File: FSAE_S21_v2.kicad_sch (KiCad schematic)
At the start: 75 parts

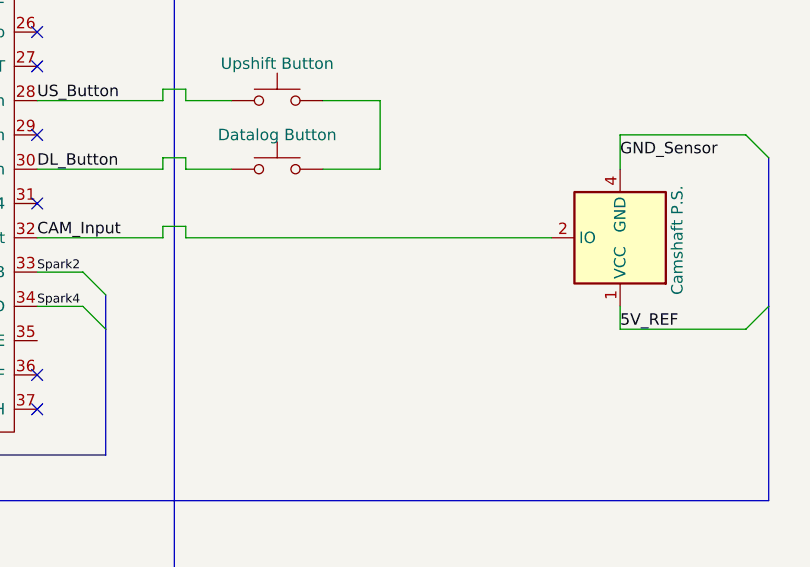
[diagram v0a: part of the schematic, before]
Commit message: added pullup resistor to cam
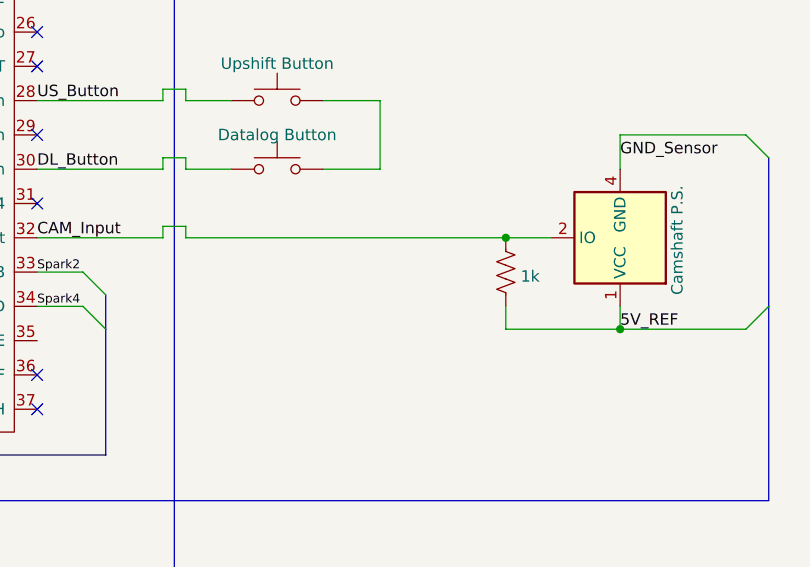
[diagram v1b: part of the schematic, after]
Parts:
- added R?: 1k, symbol Device:R_US
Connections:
- net 5V_REF: now also R?.1
- net CAM_Input: now also R?.2
- new net: F?.1, U?.~ (VCC), U?.~ (VCC), U?.~ (VCC), U?.~ (VCC)
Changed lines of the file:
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@@
   (junction (at 104.14 93.98) (diameter 0) (color 0 0 0 0)
   )
+  (junction (at 468.63 83.82) (diameter 0) (color 0 0 0 0)
+  )
   (junction (at 363.22 97.79) (diameter 0) (color 0 0 0 0)
   )
@@
   (junction (at 445.77 248.92) (diameter 0) (color 0 0 0 0)
   )
+  (junction (at 455.93 73.66) (diameter 0) (color 0 0 0 0)
+  )
   (junction (at 91.44 104.14) (diameter 0) (color 0 0 0 0)
   )
@@
     (stroke (width 0) (type default) (color 0 0 0 0))
   )
-  (wire (pts (xy 420.37 73.66) (xy 461.01 73.66))
-    (stroke (width 0) (type default) (color 0 0 0 0))
-  )
   (bus (pts (xy 345.44 38.1) (xy 345.44 36.83))
     (stroke (width 0) (type default) (color 0 0 0 0))
@@
     (stroke (width 0) (type default) (color 0 0 0 0))
   )
+  (wire (pts (xy 455.93 81.28) (xy 455.93 83.82))
+    (stroke (width 0) (type default) (color 0 0 0 0))
+  )
   (wire (pts (xy 454.66 167.64) (xy 454.66 165.1))
     (stroke (width 0) (type default) (color 0 0 0 0))
@@
     (stroke (width 0) (type default) (color 0 0 0 0))
   )
+  (wire (pts (xy 420.37 73.66) (xy 455.93 73.66))
+    (stroke (width 0) (type default) (color 0 0 0 0))
+  )
   (wire (pts (xy 105.41 160.02) (xy 110.49 160.02))
     (stroke (width 0) (type default) (color 0 0 0 0))
@@
     (stroke (width 0) (type default) (color 0 0 0 0))
   )
+  (wire (pts (xy 455.93 73.66) (xy 461.01 73.66))
+    (stroke (width 0) (type default) (color 0 0 0 0))
+  )
   (bus (pts (xy 347.98 102.87) (xy 485.14 102.87))
     (stroke (width 0) (type default) (color 0 0 0 0))
@@
     (stroke (width 0) (type default) (color 0 0 0 0))
   )
+  (wire (pts (xy 455.93 83.82) (xy 468.63 83.82))
+    (stroke (width 0) (type default) (color 0 0 0 0))
+  )
   (bus (pts (xy 417.83 222.25) (xy 438.15 222.25))
     (stroke (width 0) (type default) (color 0 0 0 0))
@@
     (pin "~")
   )
+  (symbol (lib_id "Device:R_US") (at 455.93 77.47 180) (unit 1)
+    (in_bom yes) (on_board yes) (fields_autoplaced)
+    (property "Reference" "R?" (id 0) (at 451.0745 77.47 90)
+      (effects (font (size 1.27 1.27)) hide)
+    )
+    (property "Value" "1k" (id 1) (at 457.581 77.949 0)
+      (effects (font (size 1.27 1.27)) (justify right))
+    )
+    (property "Footprint" "" (id 2) (at 454.914 77.216 90)
+      (effects (font (size 1.27 1.27)) hide)
+    )
+    (property "Datasheet" "~" (id 3) (at 455.93 77.47 0)
+      (effects (font (size 1.27 1.27)) hide)
+    )
+    (pin "1")
+    (pin "2")
+  )
   (symbol (lib_id "Device:Fuse") (at 114.3 104.14 270) (unit 1)
     (in_bom yes) (on_board yes)
@@
       (reference "M?") (unit 1) (value "Fan") (footprint "")
     )
+    (path "/975284c0-be9d-4c3a-9f49-76e7932b7001"
+      (reference "R?") (unit 1) (value "1k") (footprint "")
+    )
     (path "/e4d4909d-5947-443f-adb6-8e13c916b979"

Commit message: color updates!
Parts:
- F?: value Fuse (5 A?) -> Fuse (3 A)
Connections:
- new net: F?.1, U?.~ (VCC), U?.~ (VCC), U?.~ (VCC), U?.~ (VCC)
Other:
- note added: "Note: Add IMU stuff"
- note added: "Note: Add Telemetry stuff as well"
- note removed: "NOTE: CHECK WITH MASON ABOUT FUSE RATING"
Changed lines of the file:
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@@
   )
   (wire (pts (xy 118.11 104.14) (xy 128.27 104.14))
-    (stroke (width 0) (type default) (color 0 0 0 0))
+    (stroke (width 0) (type default) (color 255 0 0 1))
   )
   (wire (pts (xy 556.26 146.05) (xy 556.26 153.67))
@@
   )
   (wire (pts (xy 118.11 182.88) (xy 128.27 182.88))
-    (stroke (width 0) (type default) (color 0 0 0 0))
+    (stroke (width 0) (type default) (color 255 0 0 1))
   )
   (wire (pts (xy 420.37 118.11) (xy 420.37 119.38))
@@
   )
   (wire (pts (xy 118.11 81.28) (xy 128.27 81.28))
-    (stroke (width 0) (type default) (color 0 0 0 0))
+    (stroke (width 0) (type default) (color 255 0 0 1))
   )
   (bus (pts (xy 121.92 95.25) (xy 121.92 92.71))
@@
   )
   (wire (pts (xy 118.11 134.62) (xy 128.27 134.62))
-    (stroke (width 0) (type default) (color 0 0 0 0))
+    (stroke (width 0) (type default) (color 255 0 0 1))
   )
   (wire (pts (xy 163.83 24.13) (xy 163.83 35.56))
@@
   )
   (wire (pts (xy 118.11 160.02) (xy 128.27 160.02))
-    (stroke (width 0) (type default) (color 0 0 0 0))
+    (stroke (width 0) (type default) (color 255 0 0 1))
   )
   (wire (pts (xy 104.14 71.12) (xy 104.14 76.2))
@@
     )
   )
-  (text "NOTE: CHECK WITH MASON ABOUT FUSE RATING\n\n" (at 99.06 24.13 0)
-    (effects (font (size 1.27 1.27)) (justify left bottom))
-  )
   (text "NOTE: CHECK WITH PI/DISPLAY DATASHEET ABOUT FUSE RATING"
     (at 146.05 191.77 0)
@@
     (effects (font (size 1.27 1.27)) (justify left bottom))
   )
+  (text "Note: Add IMU stuff\n" (at 143.51 214.63 0)
+    (effects (font (size 1.27 1.27)) (justify left bottom))
+  )
   (text "Note: So hopefully the alternator doesn’t put out a lot of \ncurrent that would kill the electronics within the Accessory \nRelay when shut off (i mean it’s fused so should be fine?)\n\nIdea: Rather than putting PKS on the + side of battery, \nput it on negative side so when switch is off then you\nremove the ground?"
     (at 13.97 63.5 0)
@@
     (effects (font (size 1.27 1.27)) (justify left bottom))
   )
+  (text "Note: Add Telemetry stuff as well" (at 147.32 218.44 0)
+    (effects (font (size 1.27 1.27)) (justify left bottom))
+  )
   (text "NOTE: UPDATE PKS WIRING\n" (at 54.61 24.13 0)
     (effects (font (size 1.27 1.27)) (justify left bottom))
@@
     (effects (font (size 1.27 1.27)) (justify right bottom))
   )
-  (label "V_CKS" (at 104.14 172.72 0)
-    (effects (font (size 1.27 1.27)) (justify left bottom))
-  )
   (label "Oil Temp" (at 403.86 35.56 0)
     (effects (font (size 1.27 1.27)) (justify left bottom))
@@
     (effects (font (size 1 1)) (justify left bottom))
   )
+  (label "V_CKS" (at 104.14 177.8 0)
+    (effects (font (size 1.27 1.27)) (justify left bottom))
+  )
   (label "V_PKS" (at 91.44 81.28 0)
     (effects (font (size 1.27 1.27)) (justify left bottom))
@@
       (effects (font (size 1.27 1.27)) hide)
     )
-    (property "Value" "Fuse (5 A?)" (id 1) (at 111.76 24.13 90))
+    (property "Value" "Fuse (3 A)" (id 1) (at 111.76 24.13 90))
     (property "Footprint" "" (id 2) (at 111.76 24.892 90)
       (effects (font (size 1.27 1.27)) hide)
@@
     )
     (path "/37a79518-9db7-49ec-b1d5-f0bef43022e8"
-      (reference "F?") (unit 1) (value "Fuse (5 A?)") (footprint "")
+      (reference "F?") (unit 1) (value "Fuse (3 A)") (footprint "")
     )
     (path "/54a95d73-bd3e-4107-8402-74b486ffb482"

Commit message: remove main relay
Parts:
- removed F?: Fuse (7.5 A), symbol Device:Fuse
- removed K?: Main Relay, Relay_THT:Relay_SPST_StandexMeder_SIL_Form1A, symbol Relay:SILxx-1Axx-71x
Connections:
- net V_PKS: now also F?.2, F?.2
- new net: F?.1, U?.~ (VCC), U?.~ (VCC), U?.~ (VCC), U?.~ (VCC)
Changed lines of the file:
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@@
   (junction (at 223.52 63.5) (diameter 0) (color 0 0 0 0)
   )
-  (junction (at 91.44 172.72) (diameter 0) (color 0 0 0 0)
-  )
   (junction (at 571.5 153.67) (diameter 0) (color 0 0 0 0)
   )
@@
     (stroke (width 0) (type default) (color 0 0 0 0))
   )
-  (wire (pts (xy 91.44 160.02) (xy 91.44 172.72))
+  (wire (pts (xy 91.44 160.02) (xy 91.44 182.88))
     (stroke (width 0) (type default) (color 0 0 0 0))
   )
@@
     (stroke (width 0) (type default) (color 0 0 0 0))
   )
-  (wire (pts (xy 91.44 172.72) (xy 91.44 182.88))
-    (stroke (width 0) (type default) (color 0 0 0 0))
-  )
   (wire (pts (xy 441.96 58.42) (xy 441.96 66.04))
     (stroke (width 0) (type default) (color 0 0 0 0))
@@
     (stroke (width 0) (type default) (color 0 0 0 0))
   )
-  (wire (pts (xy 118.11 182.88) (xy 128.27 182.88))
-    (stroke (width 0) (type default) (color 255 0 0 1))
-  )
   (wire (pts (xy 420.37 118.11) (xy 420.37 119.38))
     (stroke (width 0) (type default) (color 0 0 0 0))
@@
     (stroke (width 0) (type default) (color 0 0 0 0))
   )
-  (wire (pts (xy 105.41 171.45) (xy 102.87 171.45))
-    (stroke (width 0) (type default) (color 0 0 0 0))
-  )
   (wire (pts (xy 295.91 200.66) (xy 295.91 204.47))
     (stroke (width 0) (type default) (color 0 0 0 0))
@@
     (stroke (width 0) (type default) (color 0 0 0 0))
   )
-  (wire (pts (xy 143.51 182.88) (xy 147.32 182.88))
-    (stroke (width 0) (type default) (color 0 0 0 0))
-  )
   (wire (pts (xy 102.87 134.62) (xy 91.44 134.62))
     (stroke (width 0) (type default) (color 0 0 0 0))
@@
     (stroke (width 0) (type default) (color 0 0 0 0))
   )
-  (wire (pts (xy 105.41 172.72) (xy 128.27 172.72))
-    (stroke (width 0) (type default) (color 0 0 0 0))
-  )
   (wire (pts (xy 488.95 134.62) (xy 495.3 134.62))
     (stroke (width 0) (type default) (color 0 0 0 0))
@@
     (stroke (width 0) (type default) (color 0 0 0 0))
   )
-  (wire (pts (xy 105.41 172.72) (xy 105.41 171.45))
-    (stroke (width 0) (type default) (color 0 0 0 0))
-  )
   (wire (pts (xy 162.56 26.67) (xy 162.56 25.4))
     (stroke (width 0) (type default) (color 0 0 0 0))
@@
     (stroke (width 0) (type default) (color 0 0 0 0))
   )
-  (wire (pts (xy 91.44 172.72) (xy 102.87 172.72))
-    (stroke (width 0) (type default) (color 0 0 0 0))
-  )
   (wire (pts (xy 365.76 77.47) (xy 374.65 77.47))
     (stroke (width 0) (type default) (color 0 0 0 0))
@@
     (stroke (width 0) (type default) (color 0 0 0 0))
   )
+  (wire (pts (xy 105.41 182.88) (xy 147.32 182.88))
+    (stroke (width 0) (type default) (color 0 0 0 0))
+  )
   (wire (pts (xy 168.91 76.2) (xy 168.91 83.82))
     (stroke (width 0) (type default) (color 0 0 0 0))
@@
     (stroke (width 0) (type default) (color 0 0 0 0))
   )
-  (wire (pts (xy 105.41 182.88) (xy 110.49 182.88))
-    (stroke (width 0) (type default) (color 0 0 0 0))
-  )
   (wire (pts (xy 417.83 118.11) (xy 420.37 118.11))
     (stroke (width 0) (type default) (color 0 0 0 0))
@@
     (stroke (width 0) (type default) (color 0 0 0 0))
   )
-  (wire (pts (xy 102.87 171.45) (xy 102.87 172.72))
-    (stroke (width 0) (type default) (color 0 0 0 0))
-  )
   (wire (pts (xy 563.88 172.72) (xy 539.75 172.72))
     (stroke (width 0) (type default) (color 0 0 0 0))
@@
     (pin "7")
   )
-  (symbol (lib_id "Relay:SILxx-1Axx-71x") (at 135.89 177.8 270) (unit 1)
-    (in_bom yes) (on_board yes)
-    (property "Reference" "K?" (id 0) (at 137.0584 186.182 0)
-      (effects (font (size 1.27 1.27)) (justify left) hide)
-    )
-    (property "Value" "Main Relay" (id 1) (at 135.89 165.735 90))
-    (property "Footprint" "Relay_THT:Relay_SPST_StandexMeder_SIL_Form1A" (id 2) (at 134.62 186.69 0)
-      (effects (font (size 1.27 1.27)) (justify left) hide)
-    )
-    (property "Datasheet" "https://standexelectronics.com/wp-content/uploads/datasheet_reed_relay_SIL.pdf" (id 3) (at 135.89 177.8 0)
-      (effects (font (size 1.27 1.27)) hide)
-    )
-    (pin "1")
-    (pin "3")
-    (pin "5")
-    (pin "7")
-  )
   (symbol (lib_id "Relay:SILxx-1Axx-71x") (at 135.89 154.94 270) (unit 1)
     (in_bom yes) (on_board yes)
@@
     (pin "2")
   )
-  (symbol (lib_id "Device:Fuse") (at 114.3 182.88 270) (unit 1)
-    (in_bom yes) (on_board yes)
-    (property "Reference" "F?" (id 0) (at 114.3 177.8762 90)
-      (effects (font (size 1.27 1.27)) hide)
-    )
-    (property "Value" "Fuse (7.5 A)" (id 1) (at 114.3 180.1876 90))
-    (property "Footprint" "" (id 2) (at 114.3 181.102 90)
-      (effects (font (size 1.27 1.27)) hide)
-    )
-    (property "Datasheet" "~" (id 3) (at 114.3 182.88 0)
-      (effects (font (size 1.27 1.27)) hide)
-    )
-    (pin "1")
-    (pin "2")
-  )
   (symbol (lib_id "power:Earth") (at 477.52 134.62 0) (unit 1)
     (in_bom yes) (on_board yes)
@@
     (pin "4")
   )
-  (symbol (lib_id "power:Earth") (at 143.51 172.72 0) (mirror y) (unit 1)
-    (in_bom yes) (on_board yes)
-    (property "Reference" "#PWR?" (id 0) (at 143.51 179.07 0)
-      (effects (font (size 1.27 1.27)) hide)
-    )
-    (property "Value" "Earth" (id 1) (at 143.51 176.53 0)
-      (effects (font (size 1.27 1.27)) hide)
-    )
-    (property "Footprint" "" (id 2) (at 143.51 172.72 0)
-      (effects (font (size 1.27 1.27)) hide)
-    )
-    (property "Datasheet" "~" (id 3) (at 143.51 172.72 0)
-      (effects (font (size 1.27 1.27)) hide)
-    )
-    (pin "1")
-  )
   (symbol (lib_id "power:Earth") (at 295.91 204.47 0) (unit 1)
     (in_bom yes) (on_board yes) (fields_autoplaced)
@@
       (reference "#PWR?") (unit 1) (value "Earth") (footprint "")
     )
-    (path "/8940b63d-6264-4ea8-b875-01d3d5541d5d"
-      (reference "#PWR?") (unit 1) (value "Earth") (footprint "")
-    )
     (path "/8fb8272e-9b94-483f-9b3c-d220f158d29a"
       (reference "#PWR?") (unit 1) (value "Earth") (footprint "")
@@
       (reference "F?") (unit 1) (value "Fuse (10 A)") (footprint "")
     )
-    (path "/23005eac-d05d-438d-9ac9-03fa00f4888c"
-      (reference "F?") (unit 1) (value "Fuse (7.5 A)") (footprint "")
-    )
     (path "/3151118f-5209-42ca-8b02-24b69bda1d5c"
       (reference "F?") (unit 1) (value "Fuse (50 A?)") (footprint "")
@@
       (reference "K?") (unit 1) (value "Starter Relay") (footprint "Relay_THT:Relay_SPST_StandexMeder_SIL_Form1A")
     )
-    (path "/00000000-0000-0000-0000-00006035b5a3"
-      (reference "K?") (unit 1) (value "Main Relay") (footprint "Relay_THT:Relay_SPST_StandexMeder_SIL_Form1A")
-    )
     (path "/00000000-0000-0000-0000-00006035c124"

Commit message: swapped brake light switch
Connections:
- net Earth: now also SW?.2 (B); no longer D?.1 (K)
- net at SW?.1 (A): now also D?.1 (K); no longer F?.1
- net at D?.2 (A): now also F?.1; no longer SW?.2 (B)
- new net: F?.1, U?.~ (VCC), U?.~ (VCC), U?.~ (VCC), U?.~ (VCC)
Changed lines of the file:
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@@
     (stroke (width 0) (type default) (color 0 0 0 0))
   )
-  (wire (pts (xy 121.92 35.56) (xy 115.57 35.56))
+  (wire (pts (xy 130.81 35.56) (xy 127 35.56))
     (stroke (width 0) (type default) (color 255 0 0 1))
   )
@@
     (stroke (width 0) (type default) (color 0 0 0 0))
   )
-  (wire (pts (xy 132.08 35.56) (xy 138.43 35.56))
-    (stroke (width 0) (type default) (color 255 0 0 1))
-  )
   (wire (pts (xy 349.25 119.38) (xy 417.83 119.38))
     (stroke (width 0) (type default) (color 0 0 0 0))
@@
     (stroke (width 0) (type default) (color 0 0 0 0))
   )
+  (wire (pts (xy 140.97 35.56) (xy 147.32 35.56))
+    (stroke (width 0) (type default) (color 0 0 0 0))
+  )
   (wire (pts (xy 359.41 158.75) (xy 359.41 179.07))
     (stroke (width 0) (type default) (color 0 0 0 0))
@@
     (stroke (width 0) (type default) (color 0 0 0 0))
   )
-  (wire (pts (xy 146.05 35.56) (xy 147.32 35.56))
-    (stroke (width 0) (type default) (color 0 0 0 0))
-  )
   (wire (pts (xy 554.99 199.39) (xy 554.99 203.2))
     (stroke (width 0) (type default) (color 0 0 0 0))
@@
     (stroke (width 0) (type default) (color 0 0 0 0))
   )
+  (wire (pts (xy 119.38 35.56) (xy 115.57 35.56))
+    (stroke (width 0) (type default) (color 255 0 0 1))
+  )
   (wire (pts (xy 104.14 93.98) (xy 104.14 124.46))
     (stroke (width 0) (type default) (color 0 0 0 0))
@@
     (pin "2")
   )
-  (symbol (lib_id "Switch:SW_SPST") (at 127 35.56 0) (unit 1)
+  (symbol (lib_id "Switch:SW_SPST") (at 135.89 35.56 0) (unit 1)
     (in_bom yes) (on_board yes)
-    (property "Reference" "SW?" (id 0) (at 127 29.591 0)
+    (property "Reference" "SW?" (id 0) (at 135.89 29.591 0)
       (effects (font (size 1.27 1.27)) hide)
     )
-    (property "Value" "Brake Light Switch" (id 1) (at 127 38.1 0))
-    (property "Footprint" "" (id 2) (at 127 35.56 0)
+    (property "Value" "Brake Light Switch" (id 1) (at 139.7 31.75 0))
+    (property "Footprint" "" (id 2) (at 135.89 35.56 0)
       (effects (font (size 1.27 1.27)) hide)
     )
-    (property "Datasheet" "~" (id 3) (at 127 35.56 0)
+    (property "Datasheet" "~" (id 3) (at 135.89 35.56 0)
       (effects (font (size 1.27 1.27)) hide)
     )
@@
     (pin "2")
   )
-  (symbol (lib_id "Device:LED") (at 142.24 35.56 180) (unit 1)
+  (symbol (lib_id "Device:LED") (at 123.19 35.56 180) (unit 1)
     (in_bom yes) (on_board yes)
-    (property "Reference" "D?" (id 0) (at 142.4178 29.083 0)
+    (property "Reference" "D?" (id 0) (at 123.3678 29.083 0)
       (effects (font (size 1.27 1.27)) hide)
     )
-    (property "Value" "Brake Light" (id 1) (at 142.4178 31.4198 0))
-    (property "Footprint" "" (id 2) (at 142.24 35.56 0)
+    (property "Value" "Brake Light" (id 1) (at 123.3678 31.4198 0))
+    (property "Footprint" "" (id 2) (at 123.19 35.56 0)
       (effects (font (size 1.27 1.27)) hide)
     )
-    (property "Datasheet" "~" (id 3) (at 142.24 35.56 0)
+    (property "Datasheet" "~" (id 3) (at 123.19 35.56 0)
       (effects (font (size 1.27 1.27)) hide)
     )

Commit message: added canbus stuff and fuses n stuff idk
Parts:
- added J?: RPi CANBUS, symbol Connector_Generic:Conn_01x02
- added J?: IMU CANBus, symbol Connector_Generic:Conn_01x02
- added SW?: Neutral Switch, symbol Switch:SW_Push
- F?: value Fuse (1 A?) -> Fuse (3-5 A)
- F?: value Fuse (50 A?) -> Fuse (50 A)
- F?: value Fuse (50 A) -> Fuse (50 A) ig
- J?: value Dash? -> Raspberry Pi/Buck Converter
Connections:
- net CANH: now also J?.2 (Pin_2), J?.2 (Pin_2)
- net CANL: now also J?.1 (Pin_1), J?.1 (Pin_1)
- net Earth: now also SW?.2, SW?.2, SW?.2
- net at U?.31 (PT4): now also SW?.1
- new net: F?.1, U?.~ (VCC), U?.~ (VCC), U?.~ (VCC), U?.~ (VCC)
- no-connect marks 57 -> 56
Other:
- note removed: "NOTE: CHECK WITH PI/DISPLAY DATASHEET ABOUT FUSE RATING"
